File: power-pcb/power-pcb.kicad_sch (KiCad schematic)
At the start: 0 parts

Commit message: power-pcb: update project metadata
Also added project code, name and version to silkscreen in the board
layout.
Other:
- title: (none) -> Main page

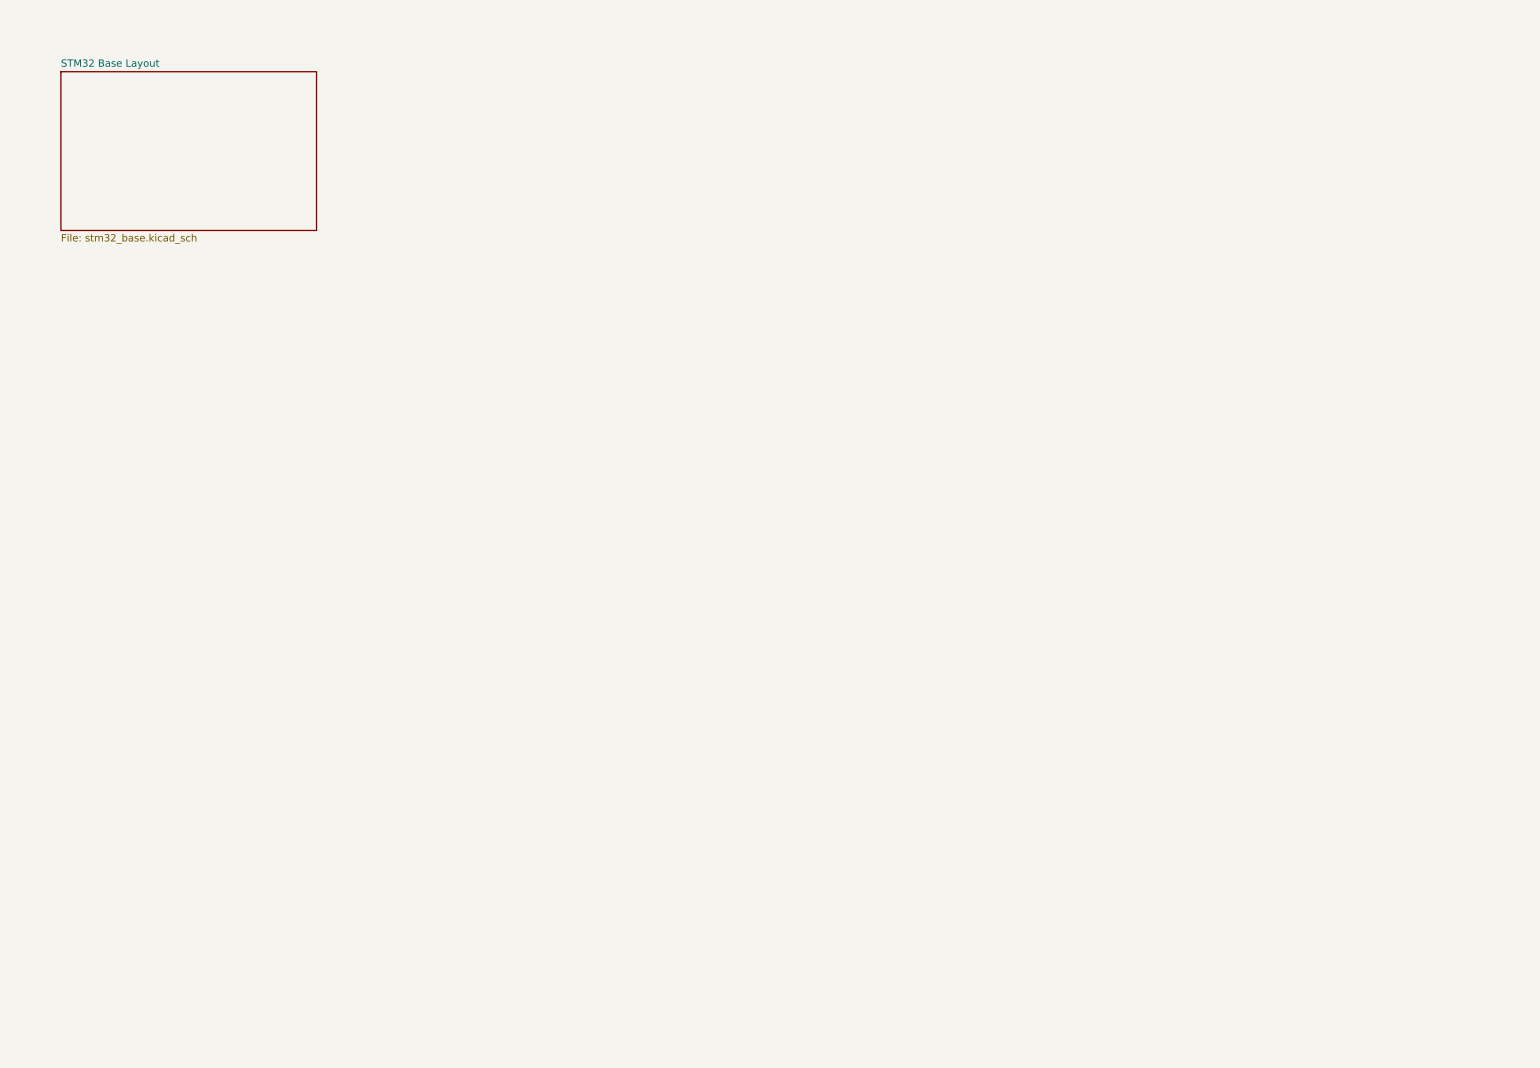
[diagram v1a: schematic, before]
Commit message: power-pcb: complete schematic
Missing some part numbers, footprints and JLCPCB codes.
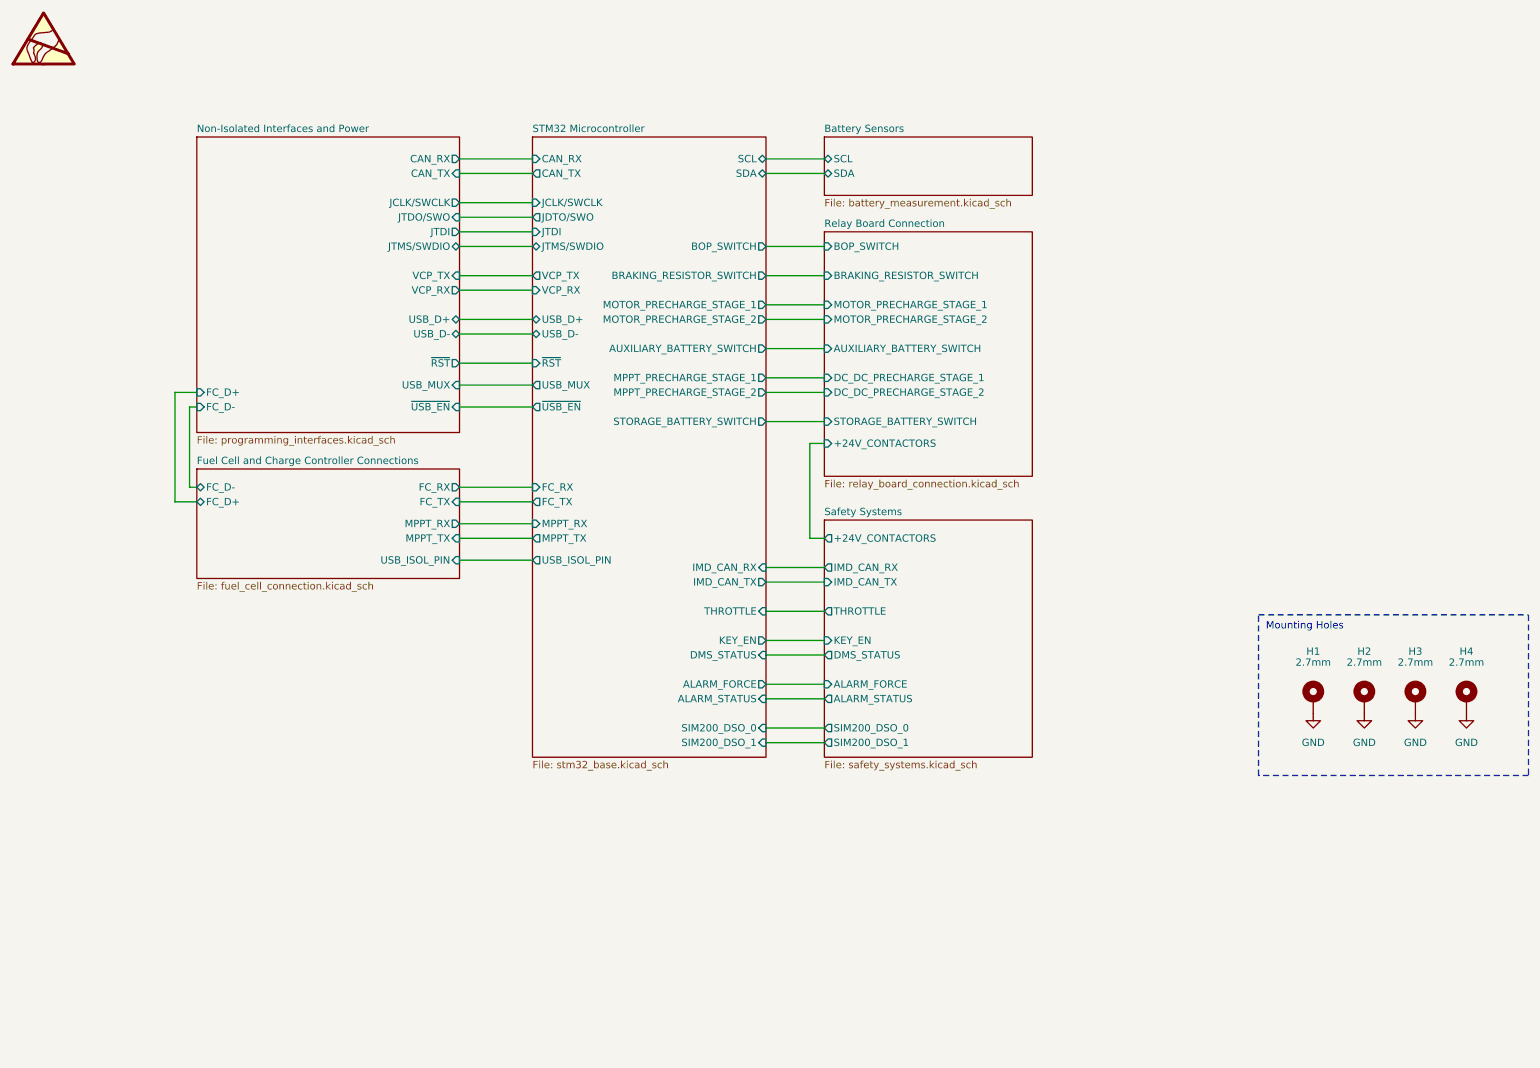
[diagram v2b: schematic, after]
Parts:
- added H1, H2, H3, H4: 2.7mm, MountingHole:MountingHole_2.7mm_Pad, symbol Mechanical:MountingHole_Pad
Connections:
- new net GND: H1.1, H2.1, H3.1, H4.1
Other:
- sheet STM32 Base Layout renamed STM32 Microcontroller
- added sheet Battery Sensors (battery_measurement.kicad_sch)
- added sheet Fuel Cell and Charge Controller Connections (fuel_cell_connection.kicad_sch)
- added sheet Non-Isolated Interfaces and Power (programming_interfaces.kicad_sch)
- added sheet Relay Board Connection (relay_board_connection.kicad_sch)
- added sheet Safety Systems (safety_systems.kicad_sch)
- sheet STM32 Microcontroller ports: added ALARM_FORCE, ALARM_STATUS, AUXILIARY_BATTERY_SWITCH, BOP_SWITCH, BRAKING_RESISTOR_SWITCH, CAN_RX, CAN_TX, DMS_STATUS, FC_RX, FC_TX, IMD_CAN_RX, IMD_CAN_TX, JCLK/SWCLK, JDTO/SWO, JTDI, JTMS/SWDIO, KEY_EN, MOTOR_PRECHARGE_STAGE_1, MOTOR_PRECHARGE_STAGE_2, MPPT_PRECHARGE_STAGE_1, MPPT_PRECHARGE_STAGE_2, MPPT_RX, MPPT_TX, SCL, SDA, SIM200_DSO_0, SIM200_DSO_1, STORAGE_BATTERY_SWITCH, THROTTLE, USB_D+, USB_D-, USB_ISOL_PIN, USB_MUX, VCP_RX, VCP_TX, ~{RST}, ~{USB_EN}; removed none
- note added: "Mounting Holes"
- title: Main page -> Overview

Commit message: power-pcb: finish schematic pages 1 to 7
- overview
- non-isolated interfaces + power
- stm32 microcontroller
- relay board connection
- battery sensors
- 48v i-v sensing (x2)
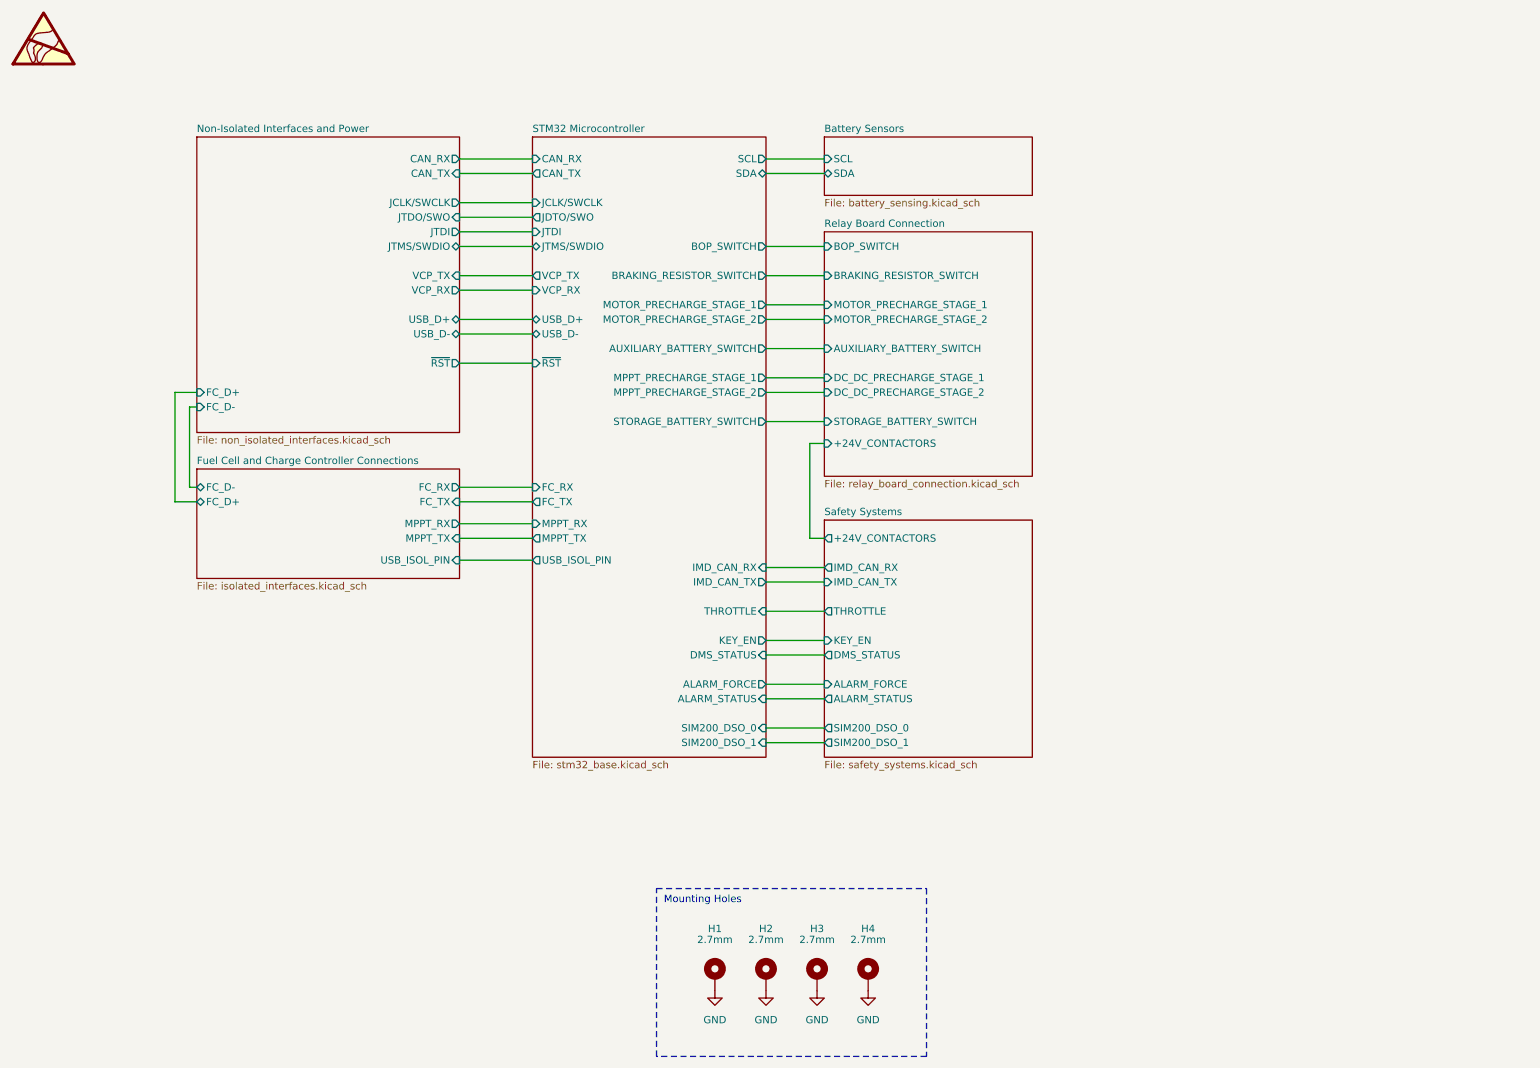
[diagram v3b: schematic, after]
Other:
- sheet Battery Sensors: file battery_measurement.kicad_sch -> battery_sensing.kicad_sch
- sheet Fuel Cell and Charge Controller Connections: file fuel_cell_connection.kicad_sch -> isolated_interfaces.kicad_sch
- sheet Non-Isolated Interfaces and Power: file programming_interfaces.kicad_sch -> non_isolated_interfaces.kicad_sch
- sheet Non-Isolated Interfaces and Power ports: added none; removed USB_MUX, ~{USB_EN}
- sheet STM32 Microcontroller ports: added none; removed USB_MUX, ~{USB_EN}
- moved on the sheet: H1, H2, H3, H4

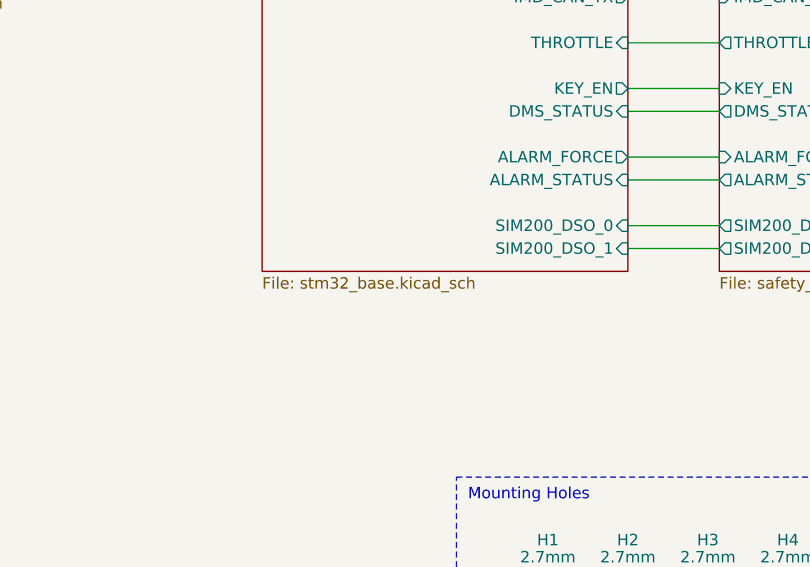
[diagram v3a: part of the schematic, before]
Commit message: power-pcb: remove unused sheets
After renaming, KiCad left the old sheets, but they were never
referenced.
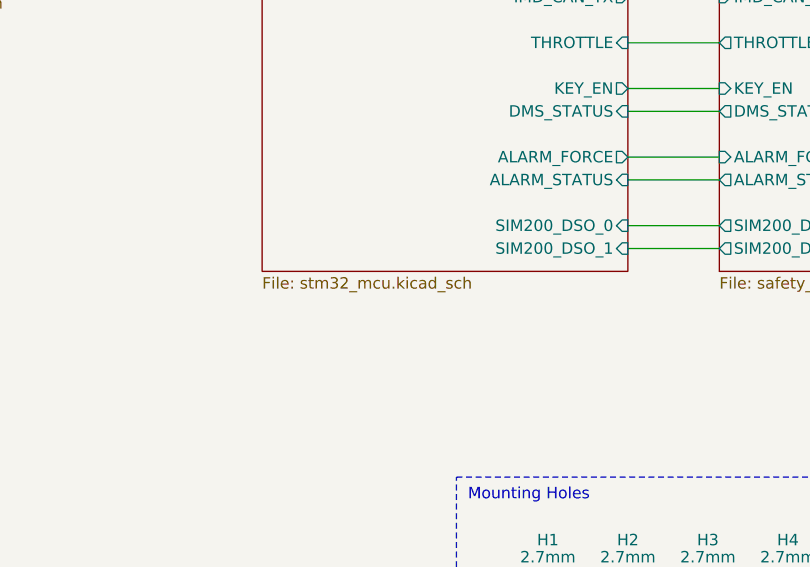
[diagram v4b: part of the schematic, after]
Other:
- sheet STM32 Microcontroller: file stm32_base.kicad_sch -> stm32_mcu.kicad_sch
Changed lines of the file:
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@@
 			)
 		)
-		(property "Sheetfile" "stm32_base.kicad_sch"
+		(property "Sheetfile" "stm32_mcu.kicad_sch"
 			(at 106.68 145.3646 0)
 			(show_name no)

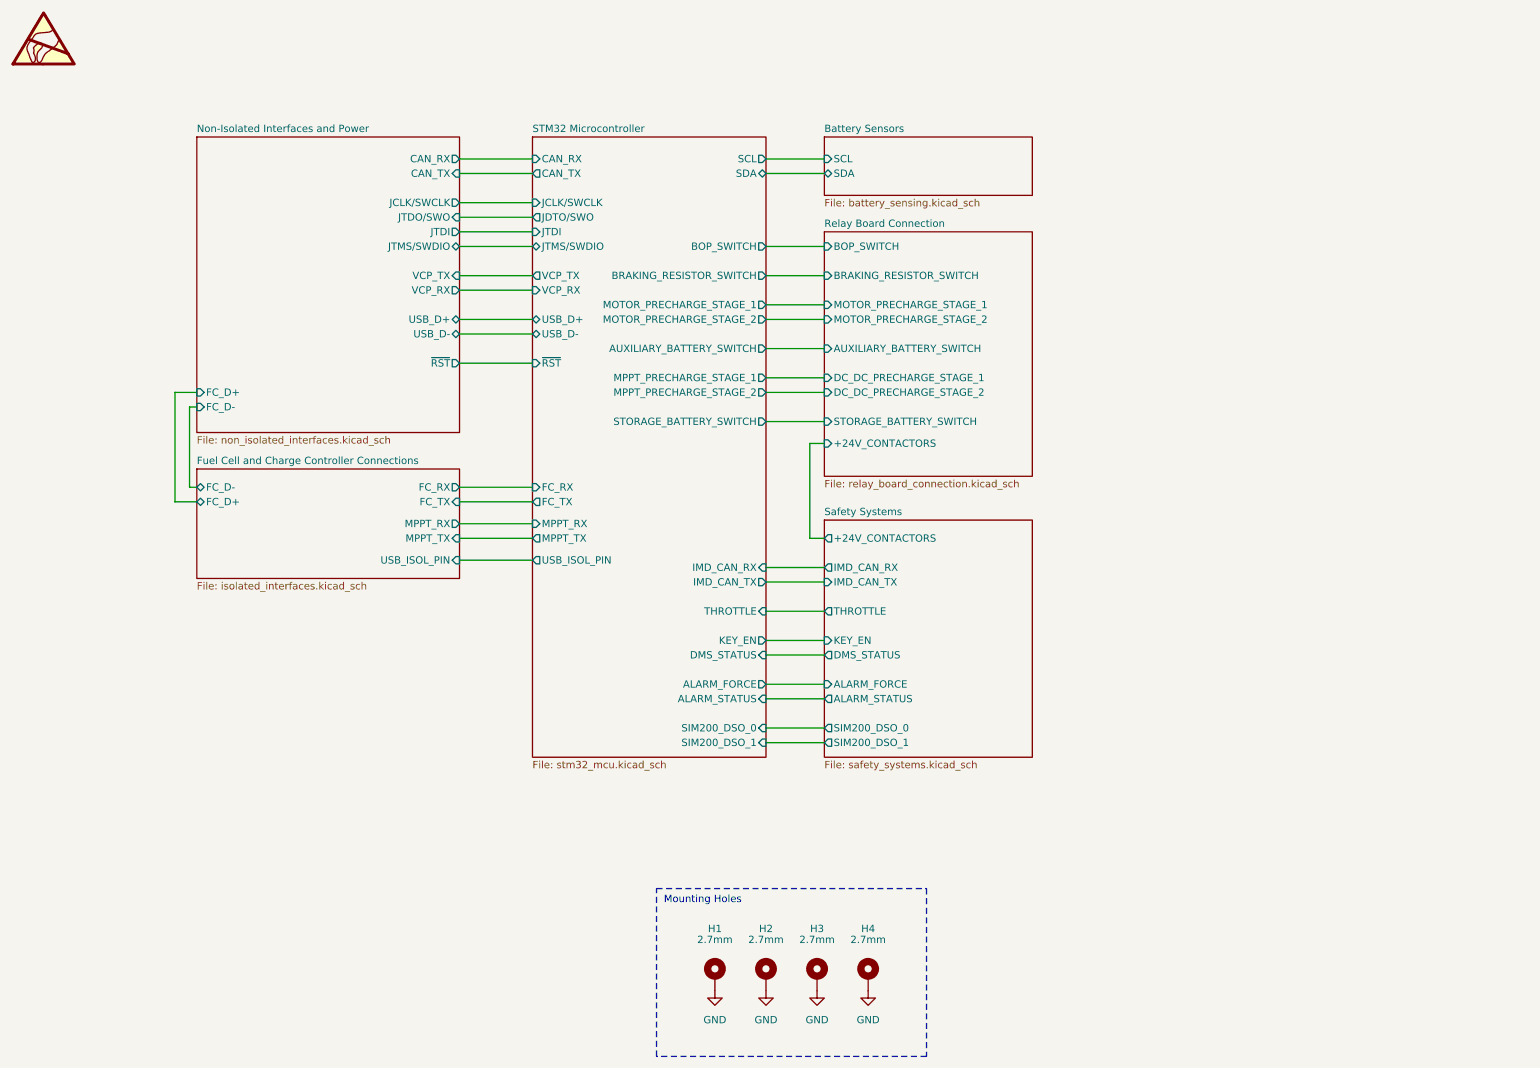
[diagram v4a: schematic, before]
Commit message: power-pcb: finish schematic layout
All parts are placed and connected, ERC passes (except for two
exclusions with comment).
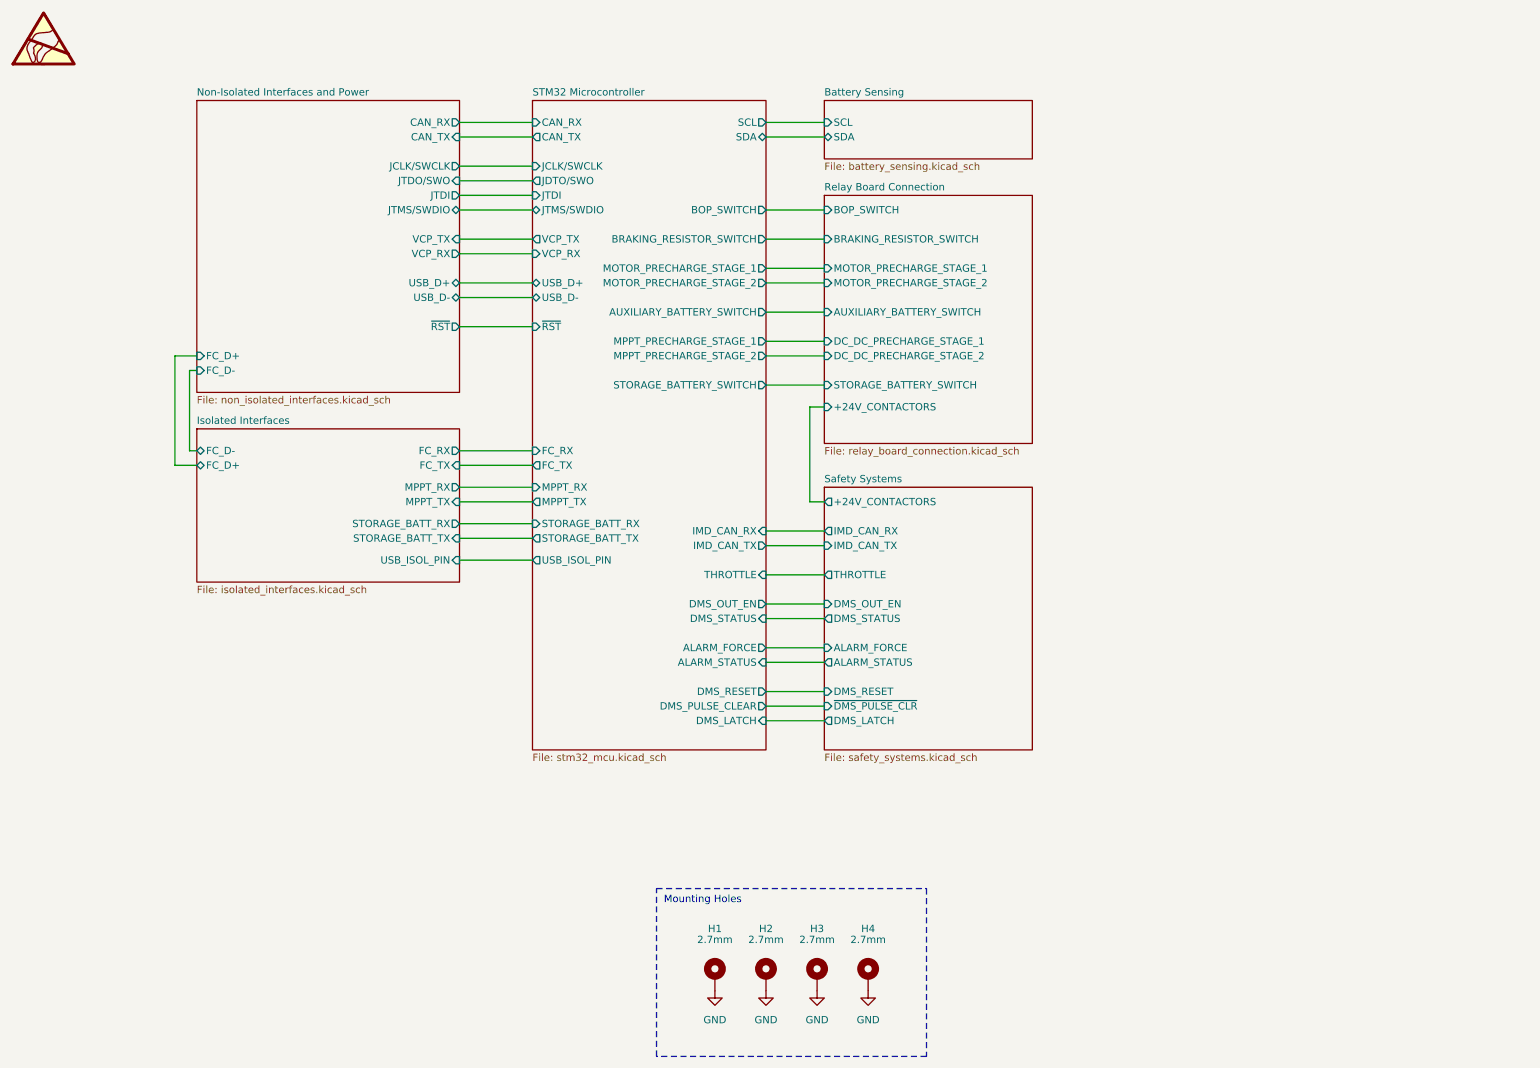
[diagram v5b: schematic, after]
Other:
- sheet Battery Sensors renamed Battery Sensing
- sheet Fuel Cell and Charge Controller Connections renamed Isolated Interfaces
- sheet Isolated Interfaces ports: added STORAGE_BATT_RX, STORAGE_BATT_TX; removed none
- sheet STM32 Microcontroller ports: added DMS_LATCH, DMS_OUT_EN, DMS_PULSE_CLEAR, DMS_RESET, STORAGE_BATT_RX, STORAGE_BATT_TX; removed KEY_EN, SIM200_DSO_0, SIM200_DSO_1
- sheet Safety Systems ports: added DMS_LATCH, DMS_OUT_EN, DMS_RESET, ~{DMS_PULSE_CLR}; removed KEY_EN, SIM200_DSO_0, SIM200_DSO_1

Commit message: power-pcb: finish assigning JLCPCB PN
Also assigned missing footprints.
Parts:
- added SYM1: SYM_ESD_Large, Symbol:ESD-Logo_13.2x12mm_SilkScreen, symbol Graphic:SYM_ESD_Large
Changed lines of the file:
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@@
 		(dnp no)
 		(fields_autoplaced yes)
-		(property "Reference" "#SYM1"
+		(property "Reference" "SYM1"
 			(at 21.59 13.97 0)
 			(hide yes)
@@
 			(project "power-pcb"
 				(path "/4b4cf3aa-c94c-4150-b9c5-35049cd71136"
-					(reference "#SYM1")
+					(reference "SYM1")
 					(unit 1)
 				)
